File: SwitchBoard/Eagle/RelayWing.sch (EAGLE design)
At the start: 29 parts, among them K1 EE2-3TNUH, K2 EE2-3TNUH, K3 EE2-3TNUH, K4 EE2-3TNUH, K5 EE2-3TNUH, U1 ULN2003ANS, U2 ULN2003ANS, U3 MCP23017SS, U4 INA219AID

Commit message: Fix contact labels.
Moved relays, labeled between pads. Cleaned up schematic around R1. Reviewed schematic and board. Design rules pass except around left mounting holes.
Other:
- moved on the sheet: R1, TB6

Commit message: Fix Ax pads, rear text.
Added bRestrict & vRestrict to address pads to keep vias & traces out of cut area. Added new shorted jumper device to prevent routing to GND via Ax. If problems, route w/ SJW then replace w/ SJW-SHORTED.

Added bottom text.
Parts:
- A0, A1: device jumper:SJW -> home:SJW-SHORTED
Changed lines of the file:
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@@
 <part name="GND1" library="supply1" library_urn="urn:adsk.eagle:library:371" deviceset="GND" device=""/>
 <part name="U4" library="home" deviceset="INA219AID" device=""/>
-<part name="A1" library="jumper" library_urn="urn:adsk.eagle:library:252" deviceset="SJ" device="W" package3d_urn="urn:adsk.eagle:package:15507/1"/>
-<part name="A0" library="jumper" library_urn="urn:adsk.eagle:library:252" deviceset="SJ" device="W" package3d_urn="urn:adsk.eagle:package:15507/1"/>
+<part name="A1" library="home" deviceset="SJW-SHORTED" device=""/>
+<part name="A0" library="home" deviceset="SJW-SHORTED" device=""/>
 <part name="R1" library="resistor" library_urn="urn:adsk.eagle:library:348" deviceset="R-US_" device="M3216" package3d_urn="urn:adsk.eagle:package:26083/1" value="0.1"/>
 <part name="C2" library="home" deviceset="MUR-1220-CAP" device="" value="MUR-1220-CAP"/>
@@
 <instance part="GND1" gate="1" x="172.72" y="40.64"/>
 <instance part="U4" gate="A" x="198.12" y="167.64"/>
-<instance part="A1" gate="1" x="160.02" y="182.88" rot="R90"/>
-<instance part="A0" gate="1" x="152.4" y="182.88" rot="R90"/>
+<instance part="A1" gate="G$1" x="160.02" y="182.88" rot="R90"/>
+<instance part="A0" gate="G$1" x="152.4" y="182.88" rot="R90"/>
 <instance part="R1" gate="G$1" x="226.06" y="142.24" smashed="yes" rot="R270">
 <attribute name="NAME" x="227.5586" y="146.05" size="1.778" layer="95" rot="R270"/>
@@
 <segment>
 <pinref part="GND3" gate="1" pin="GND"/>
-<pinref part="A0" gate="1" pin="2"/>
+<pinref part="A0" gate="G$1" pin="2"/>
 <wire x1="144.78" y1="187.96" x2="152.4" y2="187.96" width="0.1524" layer="91"/>
-<pinref part="A1" gate="1" pin="2"/>
+<pinref part="A1" gate="G$1" pin="2"/>
 <wire x1="152.4" y1="187.96" x2="160.02" y2="187.96" width="0.1524" layer="91"/>
 <junction x="152.4" y="187.96"/>
-<wire x1="152.4" y1="187.96" x2="152.4" y2="177.8" width="0.1524" layer="91"/>
-<wire x1="160.02" y1="187.96" x2="160.02" y2="177.8" width="0.1524" layer="91"/>
-<junction x="160.02" y="187.96"/>
 </segment>
 <segment>
@@
 <net name="A1" class="0">
 <segment>
-<pinref part="A1" gate="1" pin="1"/>
+<pinref part="A1" gate="G$1" pin="1"/>
 <pinref part="U4" gate="A" pin="A1"/>
 <wire x1="160.02" y1="177.8" x2="160.02" y2="172.72" width="0.1524" layer="91"/>
@@
 <net name="A0" class="0">
 <segment>
-<pinref part="A0" gate="1" pin="1"/>
+<pinref part="A0" gate="G$1" pin="1"/>
 <wire x1="152.4" y1="177.8" x2="152.4" y2="170.18" width="0.1524" layer="91"/>
 <junction x="152.4" y="170.18"/>

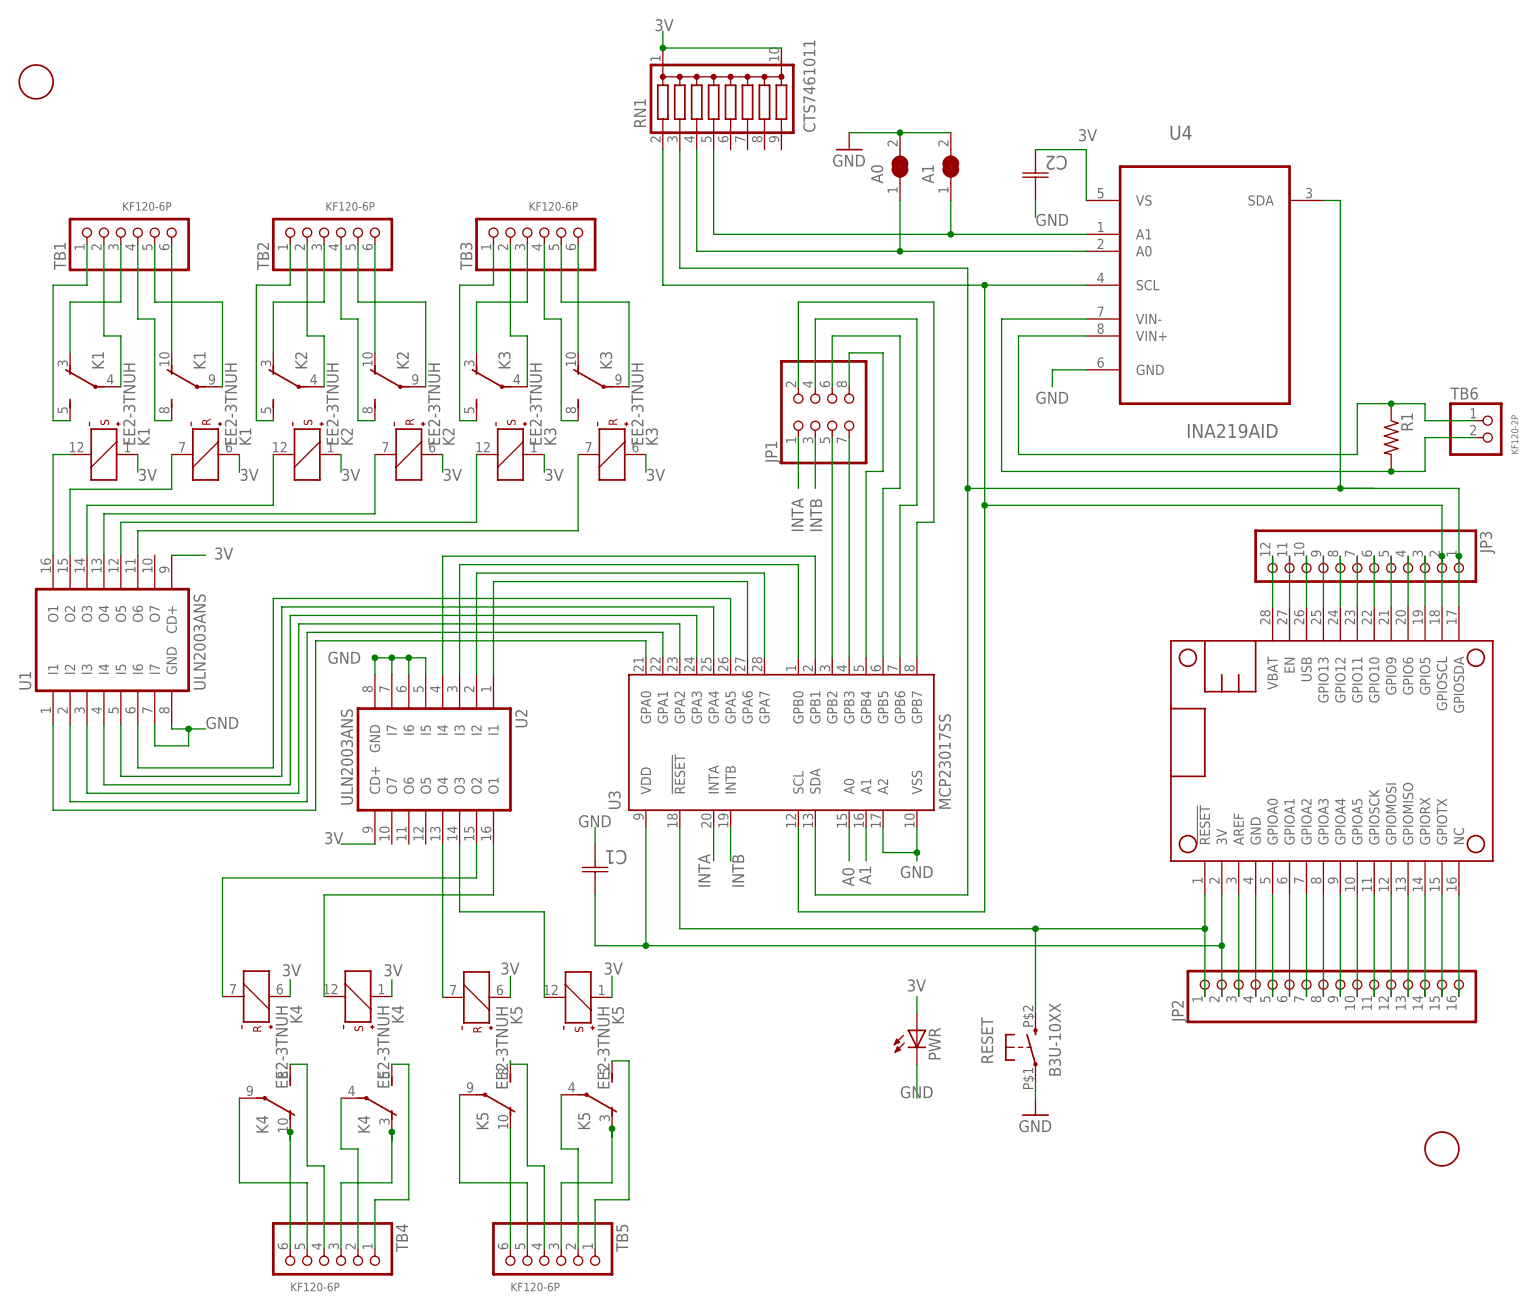
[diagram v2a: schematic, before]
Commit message: Fixed RN & GPIO A/B
New CTS746X101 device (pkg & schem).
GPIO port A=Set lines + GPIO A5-7
GPIO port B=Reset lines + GPIO B5-7
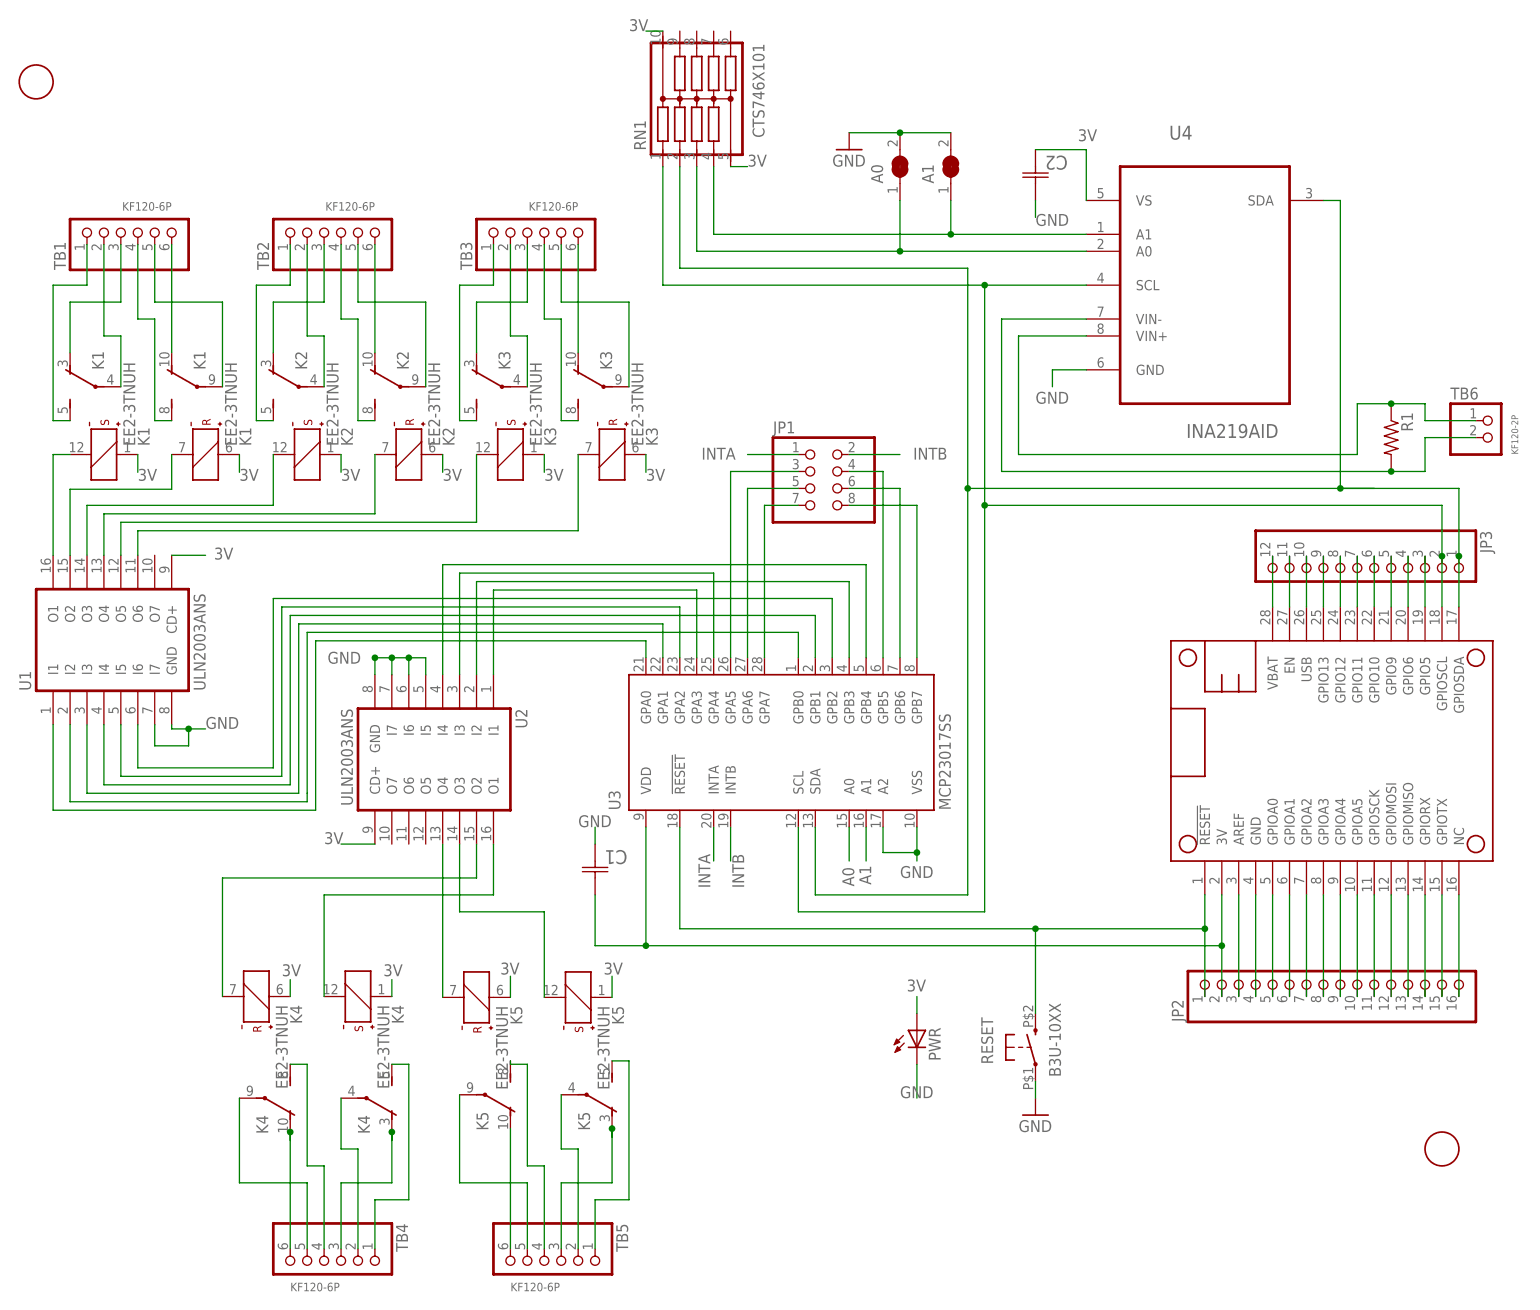
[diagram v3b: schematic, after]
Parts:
- RN1: value CTS7461011 -> CTS746X101; device home:CTS7461011 -> home:CTS746X101
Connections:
- removed net GPB2: JP1.5, U3.GPB2
- removed net GPB3: JP1.7, U3.GPB3
- new net N$31: U1.I2
- new net N$80: JP1.3, U3.GPA5
- new net N$81: JP1.5, U3.GPA6
- net 3V: now also RN1.5C; no longer RN1.1C
- net A0: now also RN1.3; no longer RN1.4
- net A1: now also RN1.4; no longer RN1.5
- net INTB: now also JP1.2; no longer JP1.3
- net N$63: now also U3.GPB0; no longer U1.I2, U3.GPA1
- net N$64: now also U3.GPA1; no longer U3.GPA2
- net N$65: now also U3.GPA2; no longer U3.GPA4
- net N$66: now also U3.GPB2; no longer U3.GPA5
- net N$67: now also U3.GPB1; no longer U3.GPA3
- net N$68: now also U3.GPA3; no longer U3.GPA6
- net N$69: now also U3.GPB3; no longer U3.GPA7
- net N$70: now also U3.GPA4; no longer U3.GPB0
- net N$71: now also U3.GPB4; no longer U3.GPB1
- net N$74: now also JP1.7, U3.GPA7; no longer JP1.8, U3.GPB4
- net N$75: now also JP1.4; no longer JP1.6
- net N$76: now also JP1.6; no longer JP1.4
- net N$77: now also JP1.8; no longer JP1.2
- net SCL: now also RN1.1; no longer RN1.2
- net SDA: now also RN1.2; no longer RN1.3
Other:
- moved on the sheet: JP1

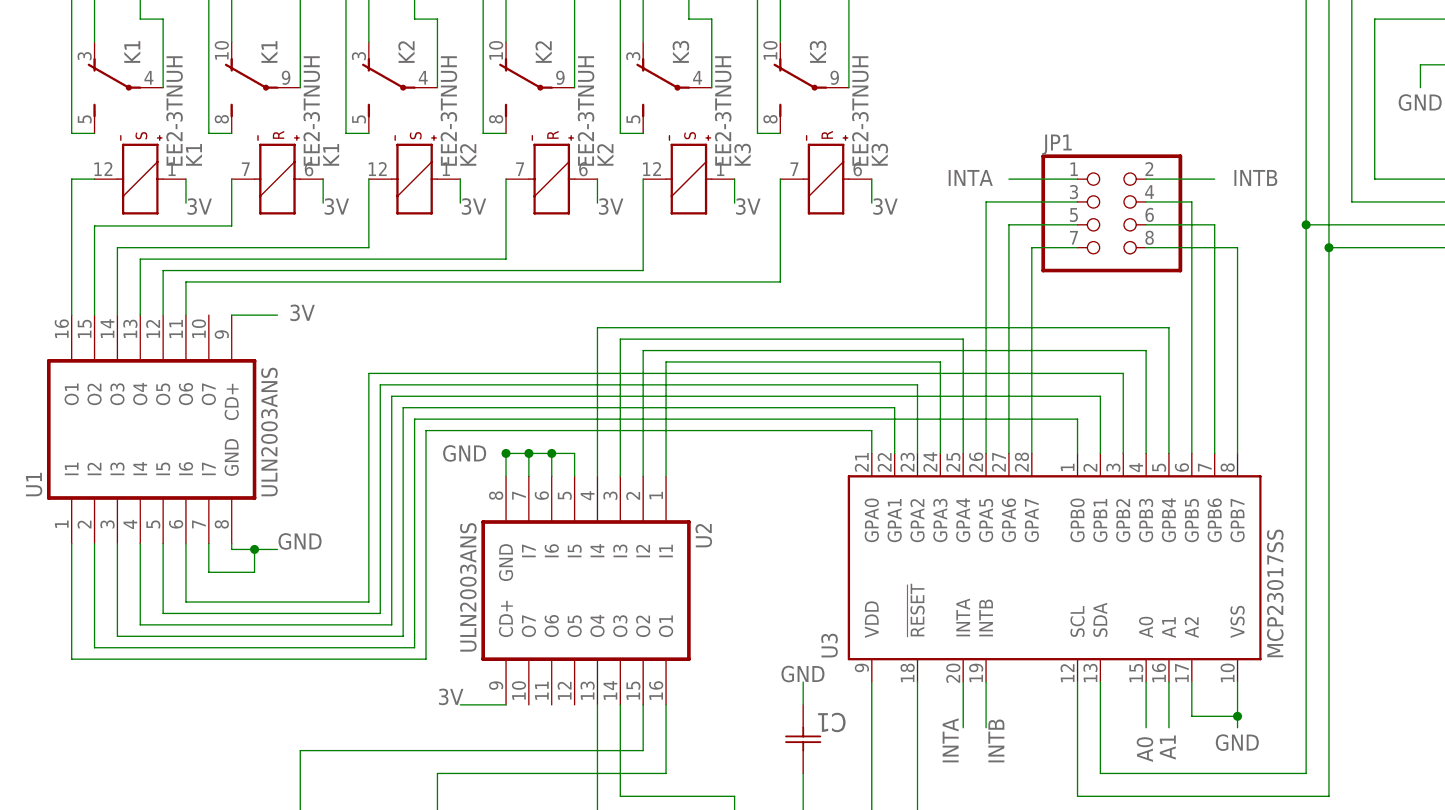
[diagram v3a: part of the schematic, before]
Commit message: Radius, labels, ERC
Corners radiused.
Relay labels added (ex Rly4).
Fixed one EDC warning.
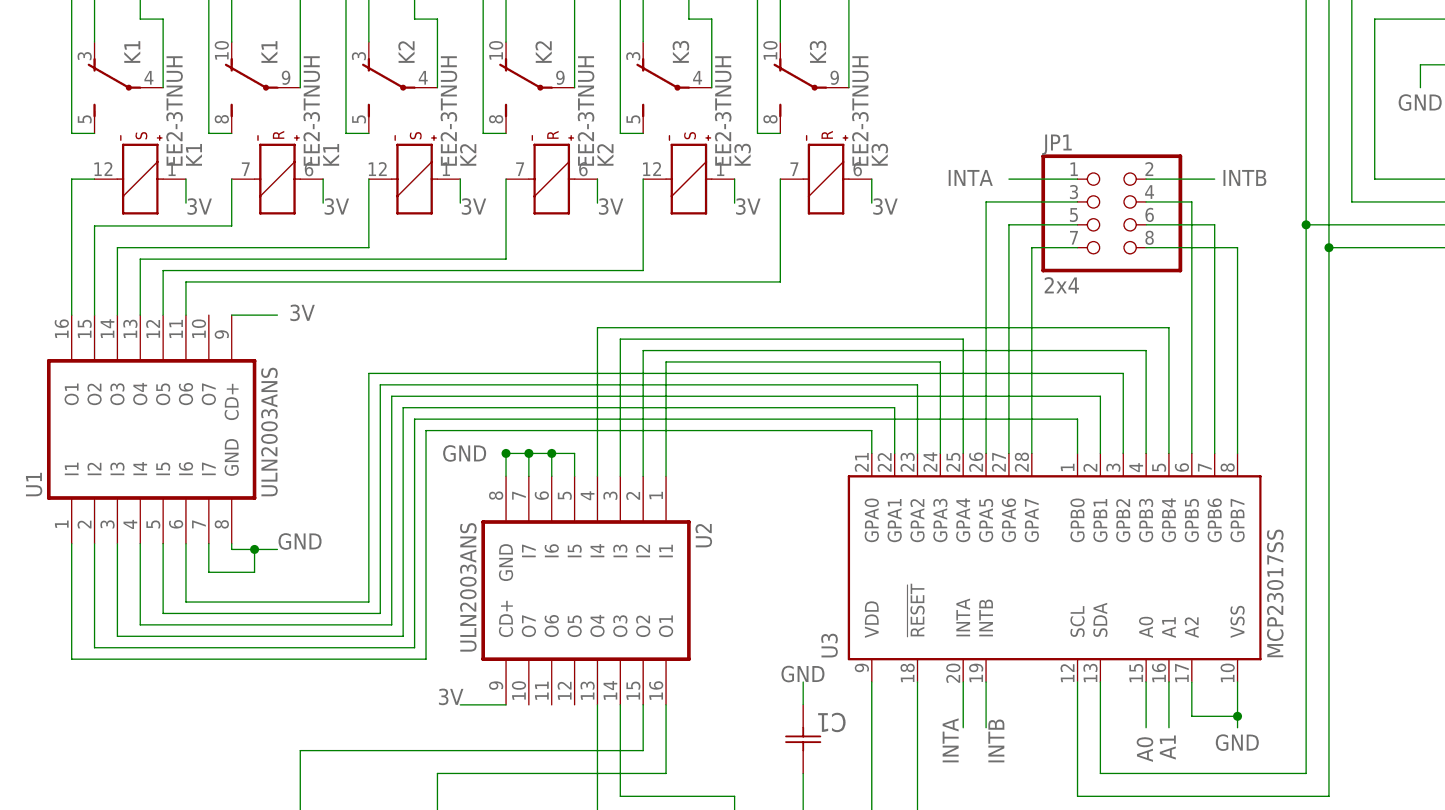
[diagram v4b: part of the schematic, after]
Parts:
- JP1: value (none) -> 2x4
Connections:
- removed net N$31: U1.I2
- net N$63: now also U1.I2

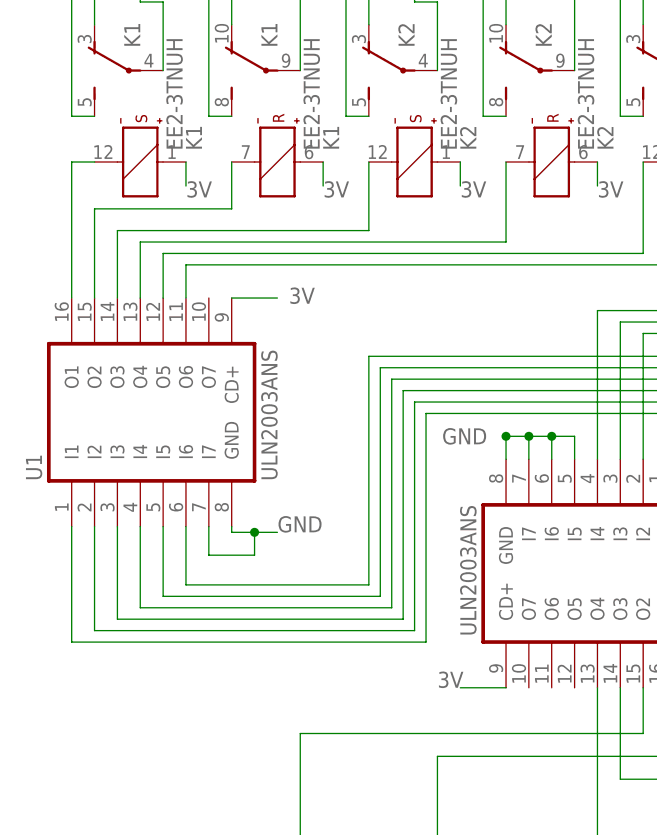
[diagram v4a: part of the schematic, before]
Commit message: Updated p/n for relay driver
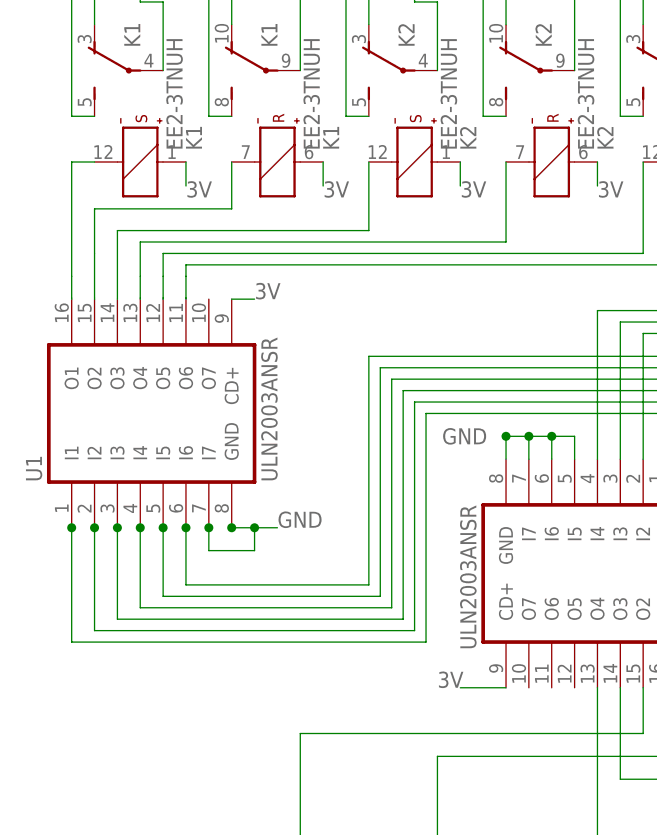
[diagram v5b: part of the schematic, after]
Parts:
- U1, U2: value ULN2003ANS -> ULN2003ANSR; device home:ULN2003ANS -> home:ULN2003ANSR
